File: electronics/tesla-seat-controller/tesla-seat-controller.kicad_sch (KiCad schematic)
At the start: 47 parts, among them J1 12V IN, J2 SWD, J3 USB-C, J8 Fan A, J9 Fan B, Q1 IPD90P03P4L-04, Q2 2N7002, Q3 2N7002, SW1 SW_Push, U1 AP63203WU, U2 STM32G0B1CBTx, Y1 ABM8-272-T3

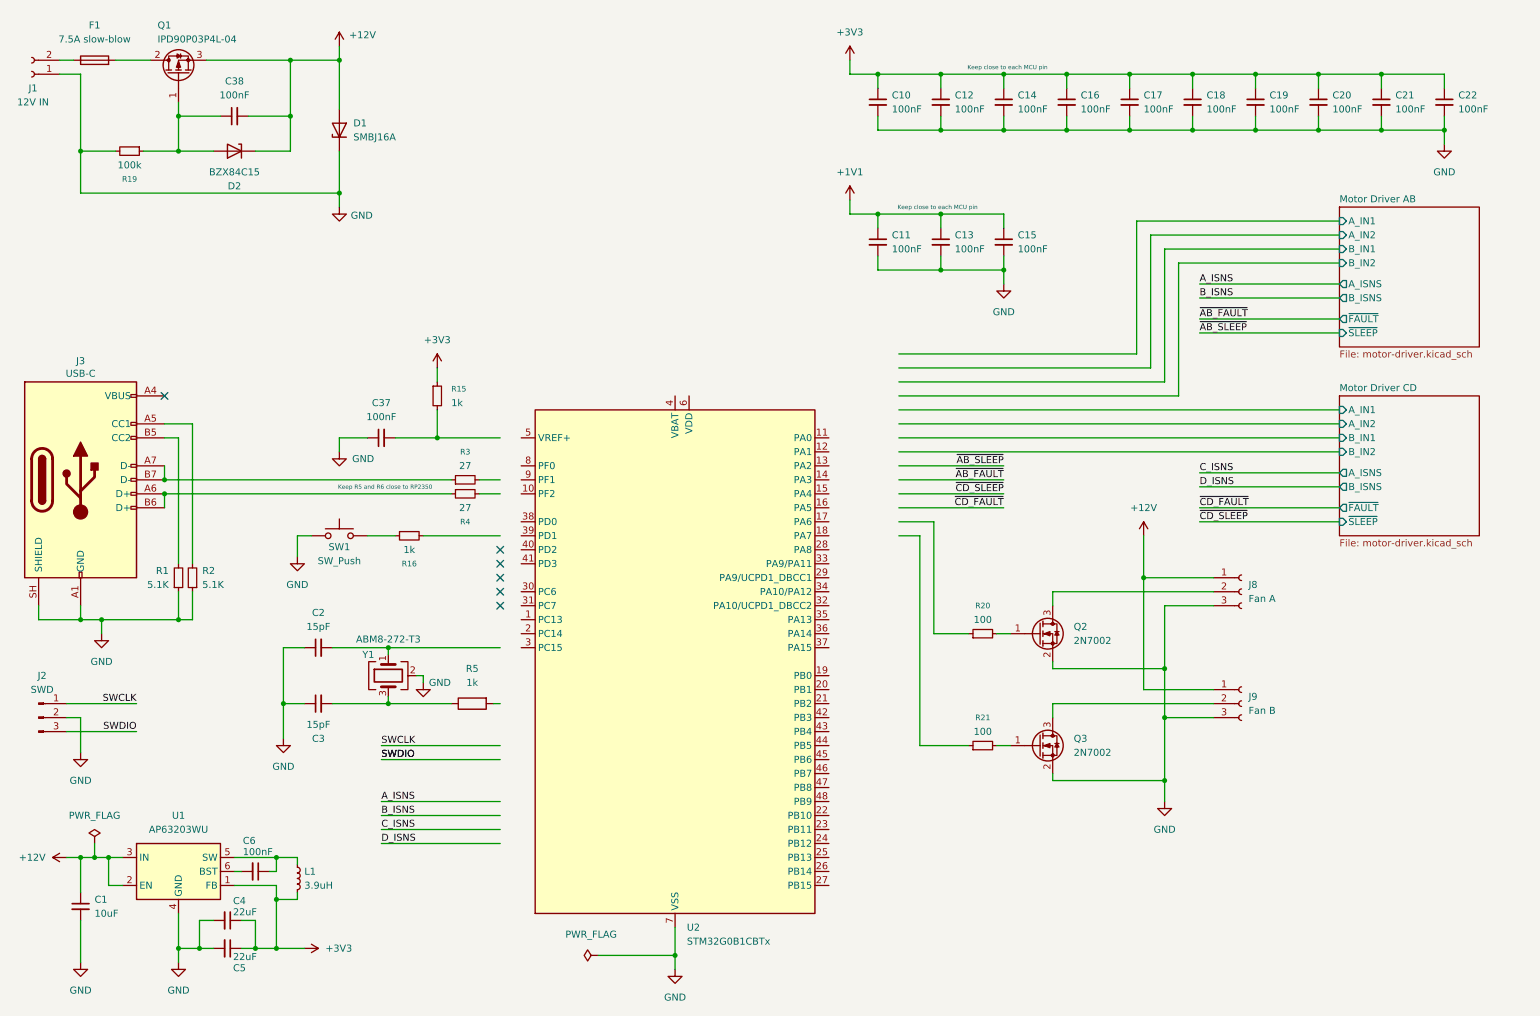
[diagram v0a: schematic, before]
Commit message: Audit fixes, DRV8262 DDV swap, 14.6A ITRIP, pin-contract tests
Schematic (all verified against datasheets, ERC clean):
- Flip D2 SMBJ16A TVS (was installed backwards, would short the 12V rail)
- C12 4.7nF -> 4.7uF (STM32 VDD bulk decoupling per DS13560)
- U2 now a proper Regulator_Switching:AP63203WU (symbol/value/lib_id were
  inconsistent AP63205WU with overridden value)
- D1 BZX84C15 -> BZX84C12 (Q1 IPD90P03P4L-04 VGS max is +5/-16V)
- Swap DRV8262DDWR -> DRV8262DDVR (top thermal pad for heatsink, 16A peak /
  10A RMS per output in dual H-bridge). Symbol pins renumbered in place per
  datasheet Table 4-1 so all wiring is untouched; EPAD pin/pad and its stub
  wires removed (DDV pad is heatsink-only). New HTSSOP44-DDV_TEX footprint
  derived from the DDW land pattern (44 pads, no thermal pad).
- ITRIP sized for max: R_IPROPI 3.09k -> 1.00k, VREF divider 19.6k -> 16.2k.
  ITRIP ~14.6A typ (13.3-16.0A tol band), deliberately under the DDV's 16A
  OCP minimum so current chopping always wins over latch-off. Also fixes
  VREF exceeding its 3.3V recommended max at DVDD tolerance extremes.
- F1: 7.5A slow-blow -> 10A mini blade fuse in Keystone 3568 holder
  (swappable rating for bring-up; motors' real stall current still unknown)

Tests:
- tests/pinmap.py: single-source-of-truth pin contract for the STM32G0B1
  (nets, timer/channel/AF claims, ADC channels, 5V-tolerance requirements)
- tests/test_pinmap.py: validates the contract against a fresh kicad-cli
  netlist export and DS13560 AF/ADC tables; catches moved pins, double-booked
  timer channels, CHx/CHxN complementary conflicts, split-timer motor pairs;
  self-test proves each checker can fail. Motor C is a documented TIM1+TIM14
  split (PA7 has no non-complementary TIM1 channel).

Cleanup: remove stray netlist/audit/report artifacts and lib backup;
ignore *.kicad_net.

Co-Authored-By: Claude Fable 5 <noreply@anthropic.com>
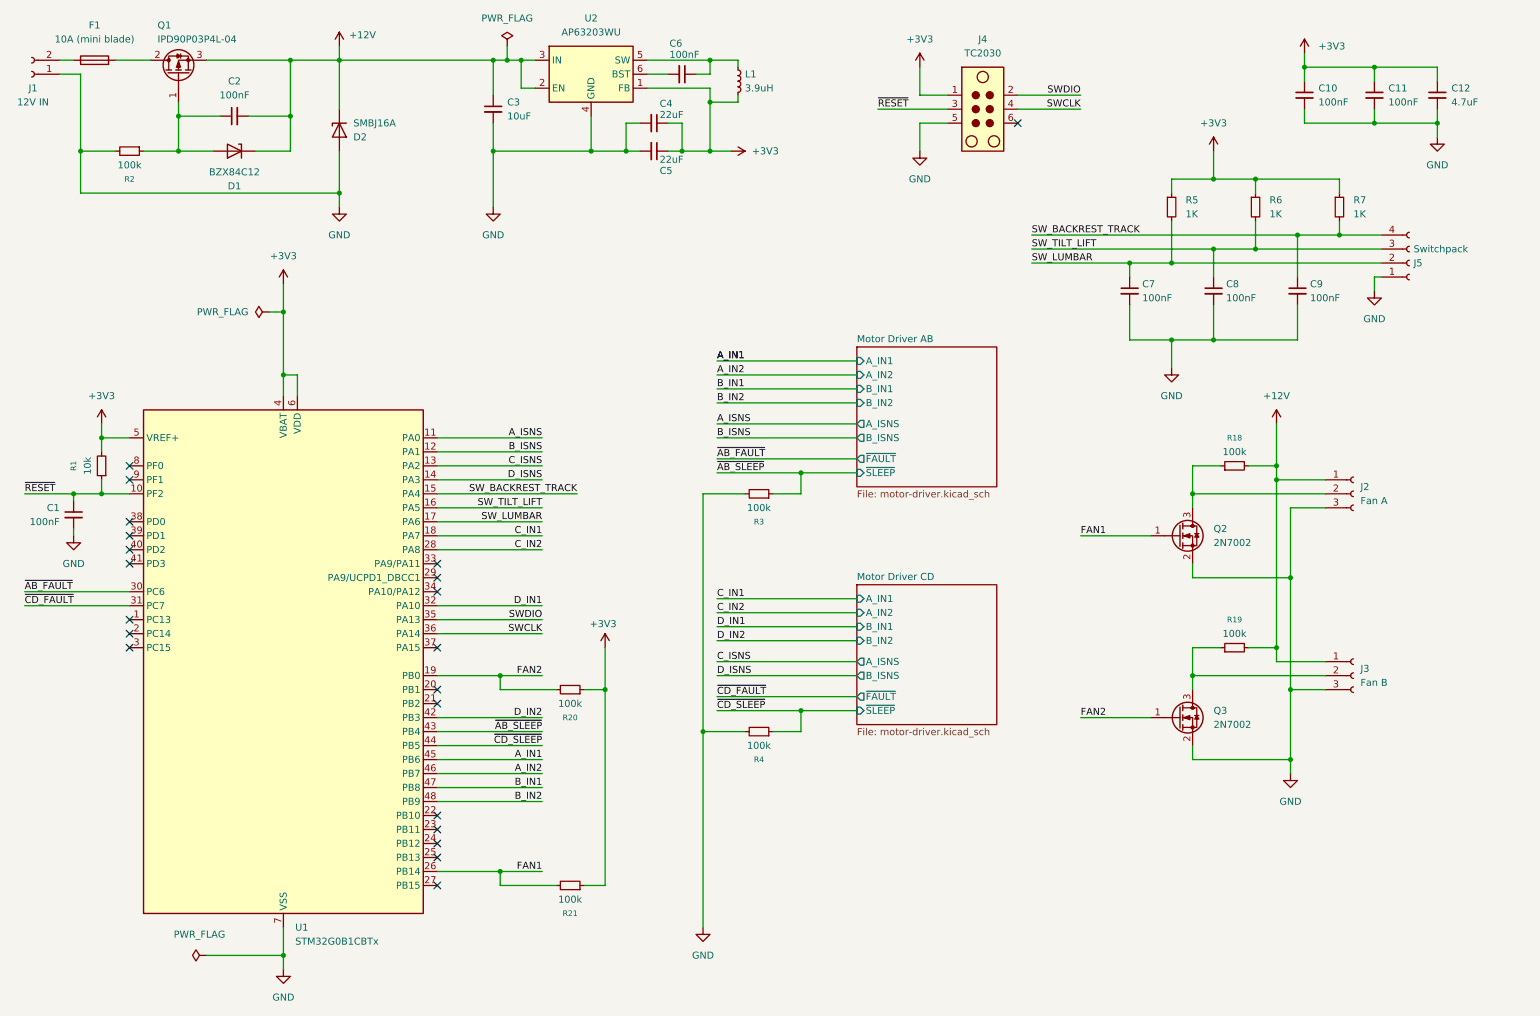
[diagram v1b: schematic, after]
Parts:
- removed C12, C14, C15, C16, C17, C18, C19, C20, C21, C22, C37: 100nF, symbol Device:C_Small
- removed C2, C3: 15pF, symbol Device:C_Small
- removed J2: SWD, symbol Connector:Conn_01x03_Pin
- removed J3: USB-C, symbol Connector:USB_C_Receptacle_USB2.0_14P
- removed R15, R16: 1k, symbol Device:R_Small
- removed R2: 5.1K, symbol Device:R_Small
- removed R5: 1k, symbol Device:R
- removed SW1: SW_Push, symbol Switch:SW_Push
- removed Y1: ABM8-272-T3, symbol Device:Crystal_GND24
- added C1: 100nF, symbol Device:C_Small
- added C7, C8, C9: 100nF, Capacitor_SMD:C_0805_2012Metric_Pad1.18x1.45mm_HandSolder, symbol Device:C_Small
- added J4: TC2030, Connector:Tag-Connect_TC2030-IDC-NL_2x03_P1.27mm_Vertical, symbol Connector:TC2030
- added J5: Switchpack, Connector_PinHeader_2.54mm:PinHeader_1x04_P2.54mm_Vertical, symbol Connector:Conn_01x04_Socket
- added R18, R19: 100k, symbol Device:R_Small
- added R5, R6, R7: 1K, Resistor_SMD:R_0805_2012Metric_Pad1.20x1.40mm_HandSolder, symbol Device:R_Small
- C12: renamed from C13; value 100nF -> 4.7uF
- D1: renamed from D2; value BZX84C15 -> BZX84C12
- F1: value 7.5A slow-blow -> 10A (mini blade); footprint (none) -> Fuse:Fuseholder_Blade_Mini_Keystone_3568
- R1: value 5.1K -> 10k
- R20, R21: value 100 -> 100k
- R3, R4: value 27 -> 100k
- U2: renamed from U1; symbol Regulator_Switching:AP63205WU -> Regulator_Switching:AP63203WU
- renumbered C38 to C2, C1 to C3, D1 to D2, J8 to J2, J9 to J3, R19 to R2, U2 to U1
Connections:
- net +1V1 is gone; now on net +3V3: C11.1, C12.1
- net +12V: now also D2.1 (K), R18.2, R19.2; no longer D2.2 (A)
- net +3V3: now also R1.2, R20.1, R21.1, U1.4 (VBAT), U1.5 (VREF+), U1.6 (VDD), J4.1, R5.1, R6.1, R7.1
- net A_ISNS: now also U1.11 (PA0)
- net B_ISNS: now also U1.12 (PA1)
- net C_ISNS: now also U1.13 (PA2)
- net D_ISNS: now also U1.14 (PA3)
- net GND: now also D2.2 (A), R3.2, R4.2, C1.2, C7.2, C8.2, C9.2, J4.5, J5.1 (Pin_1); no longer D2.1 (K), R1.1
- net SWCLK: now also U1.36 (PA14), J4.4
- net SWDIO: now also U1.35 (PA13), J4.2
- net ~{AB_FAULT}: now also U1.30 (PC6)
- net ~{AB_SLEEP}: now also R3.1, U1.43 (PB4)
- net ~{CD_FAULT}: now also U1.31 (PC7)
- net ~{CD_SLEEP}: now also R4.1, U1.44 (PB5)
- net FAN1: now reaches Q2.1 (G)
- net FAN1: now also R21.2, U1.26 (PB14); no longer R20.2
- net FAN2: now reaches Q3.1 (G)
- net FAN2: now also R20.2, U1.19 (PB0); no longer R21.2
- net at J2.2 (Pin_2), Q2.3 (D): now also R18.1
- net ~{RESET}: now reaches U1.10 (PF2)
- net ~{RESET}: now also R1.1, C1.1, J4.3
- net SW_BACKREST_TRACK: now reaches U1.15 (PA4)
- net SW_BACKREST_TRACK: now also C9.1, J5.4 (Pin_4), R7.2
- net SW_TILT_LIFT: now reaches U1.16 (PA5)
- net SW_TILT_LIFT: now also C8.1, J5.3 (Pin_3), R6.2
- net SW_LUMBAR: now reaches U1.17 (PA6)
- net SW_LUMBAR: now also C7.1, J5.2 (Pin_2), R5.2
- net C_IN1: now reaches U1.18 (PA7)
- net C_IN2: now reaches U1.28 (PA8)
- net D_IN1: now reaches U1.32 (PA10/UCPD1_DBCC2)
- net D_IN2: now reaches U1.42 (PB3)
- net A_IN1: now reaches U1.45 (PB6)
- net A_IN2: now reaches U1.46 (PB7)
- net B_IN1: now reaches U1.47 (PB8)
- net B_IN2: now reaches U1.48 (PB9)
- net at J3.2 (Pin_2), Q3.3 (D): now also R19.1
- no-connect marks 6 -> 21
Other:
- note removed: "Keep R5 and R6 close to RP2350"
- note removed: "Keep close to each MCU pin"
- moved on the sheet: C11, C12, C3, C4, C5, C6, J2, J3, L1, U1, U2

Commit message: Footprint/BOM pass: 0805 baseline for DIY reflow, side-exit connectors
- All passives 0805 (standard reflow pads, HandSolder variants normalized);
  exceptions: C3/C4/C5 in 1206 (10uF 50V, 22uF), C17/C24 upgraded
  100uF -> 220uF 35V polymer hybrid (CP_Elec 10x10.5) for the ~14.6A
  chopping level
- D1 BZX84C12 (SOT-23) -> BZT52C12 (SOD-123): same 12V zener, 2-pad
  package matches the 2-pin symbol and is easier to assemble
- D2 -> D_SMB, Q1 -> TO-252-2, L1 -> Bourns SRN6045TA (3.9uH, Isat ~5A)
- Connectors, all side-exit per harness preference: J1 XT30PW-M,
  J6-J9 XT30PW-F, J2/J3 JST S3B-XH-A, J5 JST S4B-XH-A
- README: BOM ordering notes (voltage ratings, MPNs, stencil spec)

Every component now has a footprint; ERC 0 violations; pinmap tests pass.

Co-Authored-By: Claude Fable 5 <noreply@anthropic.com>
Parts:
- C1, C10, C11, C12, C2, C6: footprint (none) -> Capacitor_SMD:C_0805_2012Metric
- C3, C4, C5: footprint (none) -> Capacitor_SMD:C_1206_3216Metric
- C7, C8, C9: footprint Capacitor_SMD:C_0805_2012Metric_Pad1.18x1.45mm_HandSolder -> Capacitor_SMD:C_0805_2012Metric
- D1: value BZX84C12 -> BZT52C12; footprint (none) -> Diode_SMD:D_SOD-123
- D2: footprint (none) -> Diode_SMD:D_SMB
- J1: footprint (none) -> Connector_AMASS:AMASS_XT30PW-M_1x02_P2.50mm_Horizontal
- J2, J3: footprint (none) -> Connector_JST:JST_XH_S3B-XH-A_1x03_P2.50mm_Horizontal
- J5: footprint Connector_PinHeader_2.54mm:PinHeader_1x04_P2.54mm_Vertical -> Connector_JST:JST_XH_S4B-XH-A_1x04_P2.50mm_Horizontal
- L1: footprint (none) -> Inductor_SMD:L_Bourns_SRN6045TA
- Q1: footprint (none) -> Package_TO_SOT_SMD:TO-252-2
- R1, R18, R19, R2, R20, R21, R3, R4: footprint (none) -> Resistor_SMD:R_0805_2012Metric
- R5, R6, R7: footprint Resistor_SMD:R_0805_2012Metric_Pad1.20x1.40mm_HandSolder -> Resistor_SMD:R_0805_2012Metric
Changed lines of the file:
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@@
 			)
 		)
-		(property "Footprint" "Capacitor_SMD:C_0805_2012Metric_Pad1.18x1.45mm_HandSolder"
+		(property "Footprint" "Capacitor_SMD:C_0805_2012Metric"
 			(at 233.68 64.77 0)
 			(hide yes)
@@
 			)
 		)
-		(property "Footprint" ""
+		(property "Footprint" "Resistor_SMD:R_0805_2012Metric"
 			(at 237.49 96.52 0)
 			(hide yes)
@@
 			)
 		)
-		(property "Footprint" ""
+		(property "Footprint" "Resistor_SMD:R_0805_2012Metric"
 			(at 36.83 39.37 0)
 			(hide yes)
@@
 			)
 		)
-		(property "Footprint" ""
+		(property "Footprint" "Resistor_SMD:R_0805_2012Metric"
 			(at 31.75 96.52 0)
 			(hide yes)
@@
 			)
 		)
-		(property "Footprint" ""
+		(property "Footprint" "Resistor_SMD:R_0805_2012Metric"
 			(at 151.13 144.78 0)
 			(hide yes)
@@
 			)
 		)
-		(property "Footprint" ""
+		(property "Footprint" "Capacitor_SMD:C_1206_3216Metric"
 			(at 132.08 39.37 0)
 			(hide yes)
@@
 			)
 		)
-		(property "Footprint" ""
+		(property "Footprint" "Capacitor_SMD:C_0805_2012Metric"
 			(at 262.89 29.21 0)
 			(hide yes)
@@
 			)
 		)
-		(property "Footprint" ""
+		(property "Footprint" "Package_TO_SOT_SMD:TO-252-2"
 			(at 43.18 20.32 0)
 			(hide yes)
@@
 			)
 		)
-		(property "Footprint" "Resistor_SMD:R_0805_2012Metric_Pad1.20x1.40mm_HandSolder"
+		(property "Footprint" "Resistor_SMD:R_0805_2012Metric"
 			(at 256.54 49.53 0)
 			(hide yes)
@@
 			)
 		)
-		(property "Footprint" ""
+		(property "Footprint" "Connector_JST:JST_XH_S3B-XH-A_1x03_P2.50mm_Horizontal"
 			(at 259.08 101.6 0)
 			(hide yes)
@@
 			)
 		)
-		(property "Footprint" ""
+		(property "Footprint" "Resistor_SMD:R_0805_2012Metric"
 			(at 116.84 172.72 0)
 			(hide yes)
@@
 			)
 		)
-		(property "Footprint" ""
+		(property "Footprint" "Capacitor_SMD:C_0805_2012Metric"
 			(at 137.16 25.4 0)
 			(hide yes)
@@
 			)
 		)
-		(property "Footprint" "Capacitor_SMD:C_0805_2012Metric_Pad1.18x1.45mm_HandSolder"
+		(property "Footprint" "Capacitor_SMD:C_0805_2012Metric"
 			(at 218.44 64.77 0)
 			(hide yes)
@@
 			)
 		)
-		(property "Footprint" ""
+		(property "Footprint" "Diode_SMD:D_SMB"
 			(at 74.93 35.56 0)
 			(hide yes)
@@
 			)
 		)
-		(property "Footprint" ""
+		(property "Footprint" "Capacitor_SMD:C_1206_3216Metric"
 			(at 102.87 31.75 0)
 			(hide yes)
@@
 			)
 		)
-		(property "Value" "BZX84C12"
+		(property "Value" "BZT52C12"
 			(at 55.88 43.18 0)
 			(show_name no)
@@
 			)
 		)
-		(property "Footprint" ""
+		(property "Footprint" "Diode_SMD:D_SOD-123"
 			(at 55.88 39.37 0)
 			(hide yes)
@@
 			)
 		)
-		(property "Footprint" ""
+		(property "Footprint" "Capacitor_SMD:C_0805_2012Metric"
 			(at 55.88 33.02 0)
 			(hide yes)
@@
 			)
 		)
-		(property "Footprint" ""
+		(property "Footprint" "Capacitor_SMD:C_1206_3216Metric"
 			(at 132.08 34.29 0)
 			(hide yes)
@@
 			)
 		)
-		(property "Footprint" ""
+		(property "Footprint" "Connector_AMASS:AMASS_XT30PW-M_1x02_P2.50mm_Horizontal"
 			(at 19.05 25.4 0)
 			(hide yes)
@@
 			)
 		)
-		(property "Footprint" ""
+		(property "Footprint" "Connector_JST:JST_XH_S3B-XH-A_1x03_P2.50mm_Horizontal"
 			(at 259.08 134.62 0)
 			(hide yes)
@@
 			)
 		)
-		(property "Footprint" ""
+		(property "Footprint" "Resistor_SMD:R_0805_2012Metric"
 			(at 116.84 137.16 0)
 			(hide yes)
@@
 			)
 		)
-		(property "Footprint" ""
+		(property "Footprint" "Resistor_SMD:R_0805_2012Metric"
 			(at 151.13 101.6 0)
 			(hide yes)
@@
 			)
 		)
-		(property "Footprint" ""
+		(property "Footprint" "Capacitor_SMD:C_0805_2012Metric"
 			(at 26.67 105.41 0)
 			(hide yes)
@@
 			)
 		)
-		(property "Footprint" "Resistor_SMD:R_0805_2012Metric_Pad1.20x1.40mm_HandSolder"
+		(property "Footprint" "Resistor_SMD:R_0805_2012Metric"
 			(at 226.06 49.53 0)
 			(hide yes)
@@
 			)
 		)
-		(property "Footprint" ""
+		(property "Footprint" "Inductor_SMD:L_Bourns_SRN6045TA"
 			(at 147.32 26.67 0)
 			(hide yes)
@@
 			)
 		)
-		(property "Footprint" "Connector_PinHeader_2.54mm:PinHeader_1x04_P2.54mm_Vertical"
+		(property "Footprint" "Connector_JST:JST_XH_S4B-XH-A_1x04_P2.50mm_Horizontal"
 			(at 269.24 59.69 0)
 			(hide yes)
@@
 			)
 		)
-		(property "Footprint" "Capacitor_SMD:C_0805_2012Metric_Pad1.18x1.45mm_HandSolder"
+		(property "Footprint" "Capacitor_SMD:C_0805_2012Metric"
 			(at 248.92 64.77 0)
 			(hide yes)
@@
 			)
 		)
-		(property "Footprint" ""
+		(property "Footprint" "Capacitor_SMD:C_0805_2012Metric"
 			(at 274.32 29.21 0)
 			(hide yes)
@@
 			)
 		)
-		(property "Footprint" ""
+		(property "Footprint" "Resistor_SMD:R_0805_2012Metric"
 			(at 237.49 129.54 0)
 			(hide yes)
@@
 			)
 		)
-		(property "Footprint" ""
+		(property "Footprint" "Capacitor_SMD:C_0805_2012Metric"
 			(at 250.19 29.21 0)
 			(hide yes)
@@
 			)
 		)
-		(property "Footprint" "Resistor_SMD:R_0805_2012Metric_Pad1.20x1.40mm_HandSolder"
+		(property "Footprint" "Resistor_SMD:R_0805_2012Metric"
 			(at 241.3 49.53 0)
 			(hide yes)

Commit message: Add schematic title blocks
Co-Authored-By: Claude Fable 5 <noreply@anthropic.com>
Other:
- title: (none) -> Tesla Seat Controller
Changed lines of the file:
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@@
 	(generator_version "10.0")
 	(paper "A4")
+	(title_block
+		(title "Tesla Seat Controller")
+		(date "2026-07-17")
+	)
 	(junction
 		(at 26.67 101.6)
